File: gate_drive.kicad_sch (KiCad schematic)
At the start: 186 parts, among them J19 Conn_01x03, J20 Conn_01x03, Q1 Q_PNP_BEC, Q2 Q_PNP_BEC, Q3 Q_PNP_BEC, Q4 Q_PNP_BEC, Q5 Q_PNP_BEC, Q6 Q_PNP_BEC, U1 EG2131, U14 INA193, U2 EG2131, U20 INA193, U21 INA193, U22 INA193, U35 INA193, U36 INA826, U37 INA193, U38 INA826, U39 INA193, U4 EG2131, U40 INA826, U41 INA193, U42 INA826, U5 EG2131, U7 EG2131, U8 EG2131

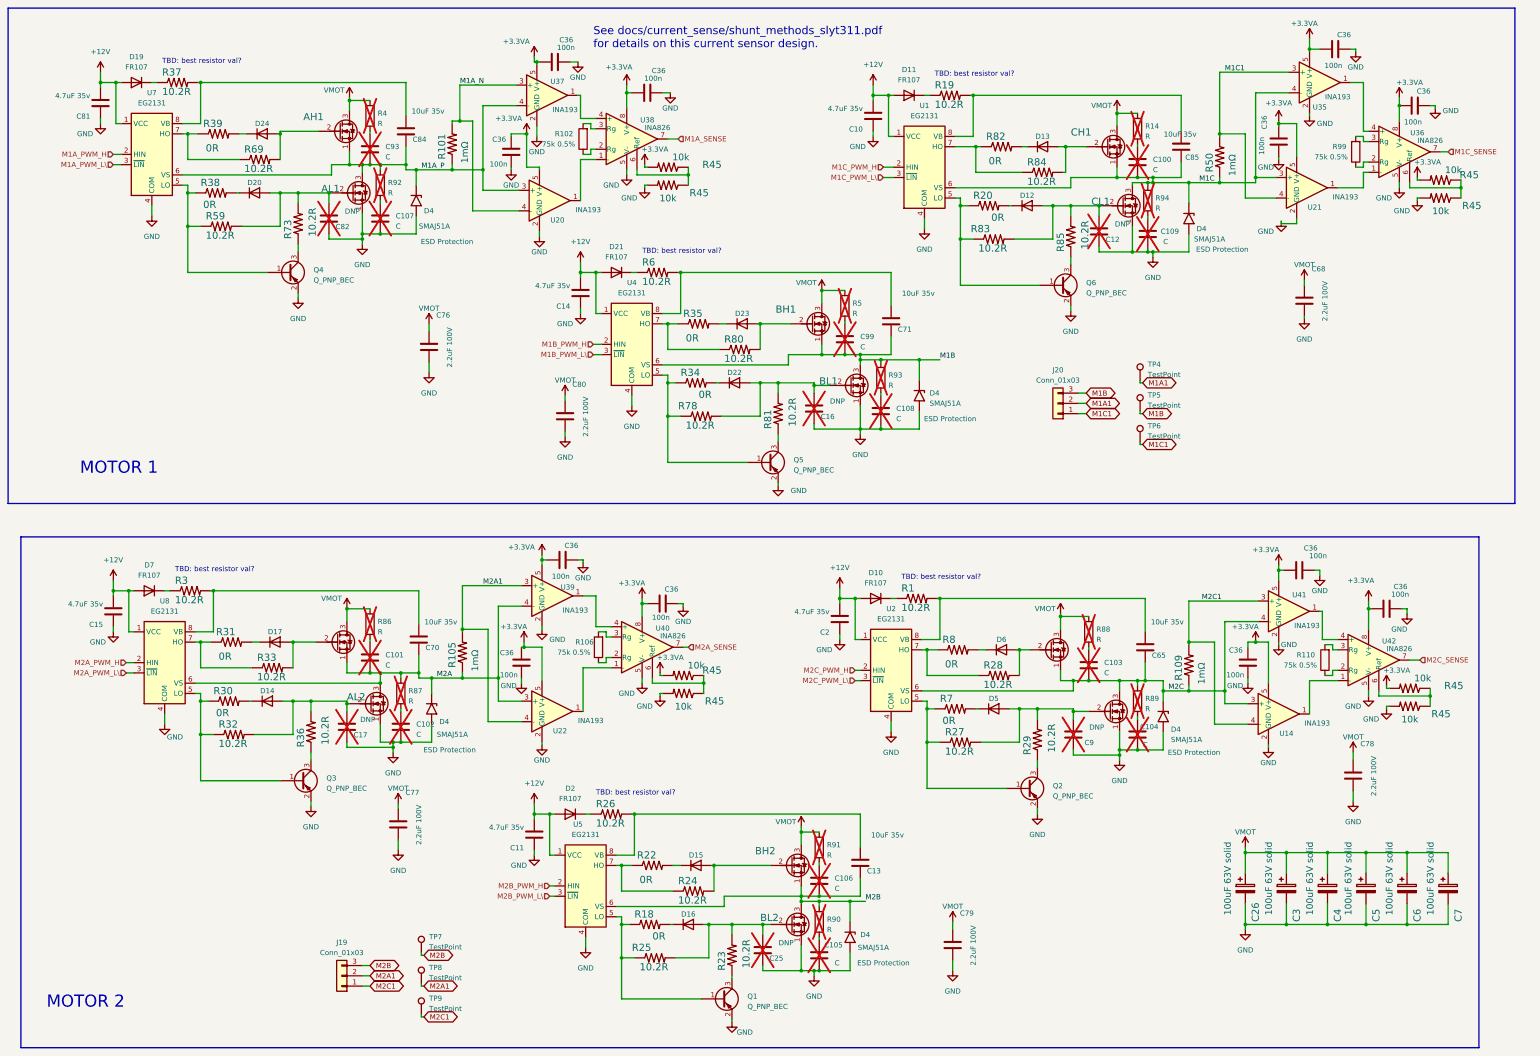
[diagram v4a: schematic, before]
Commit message: Work in progress. cleared out old traces in layout and starting fresh
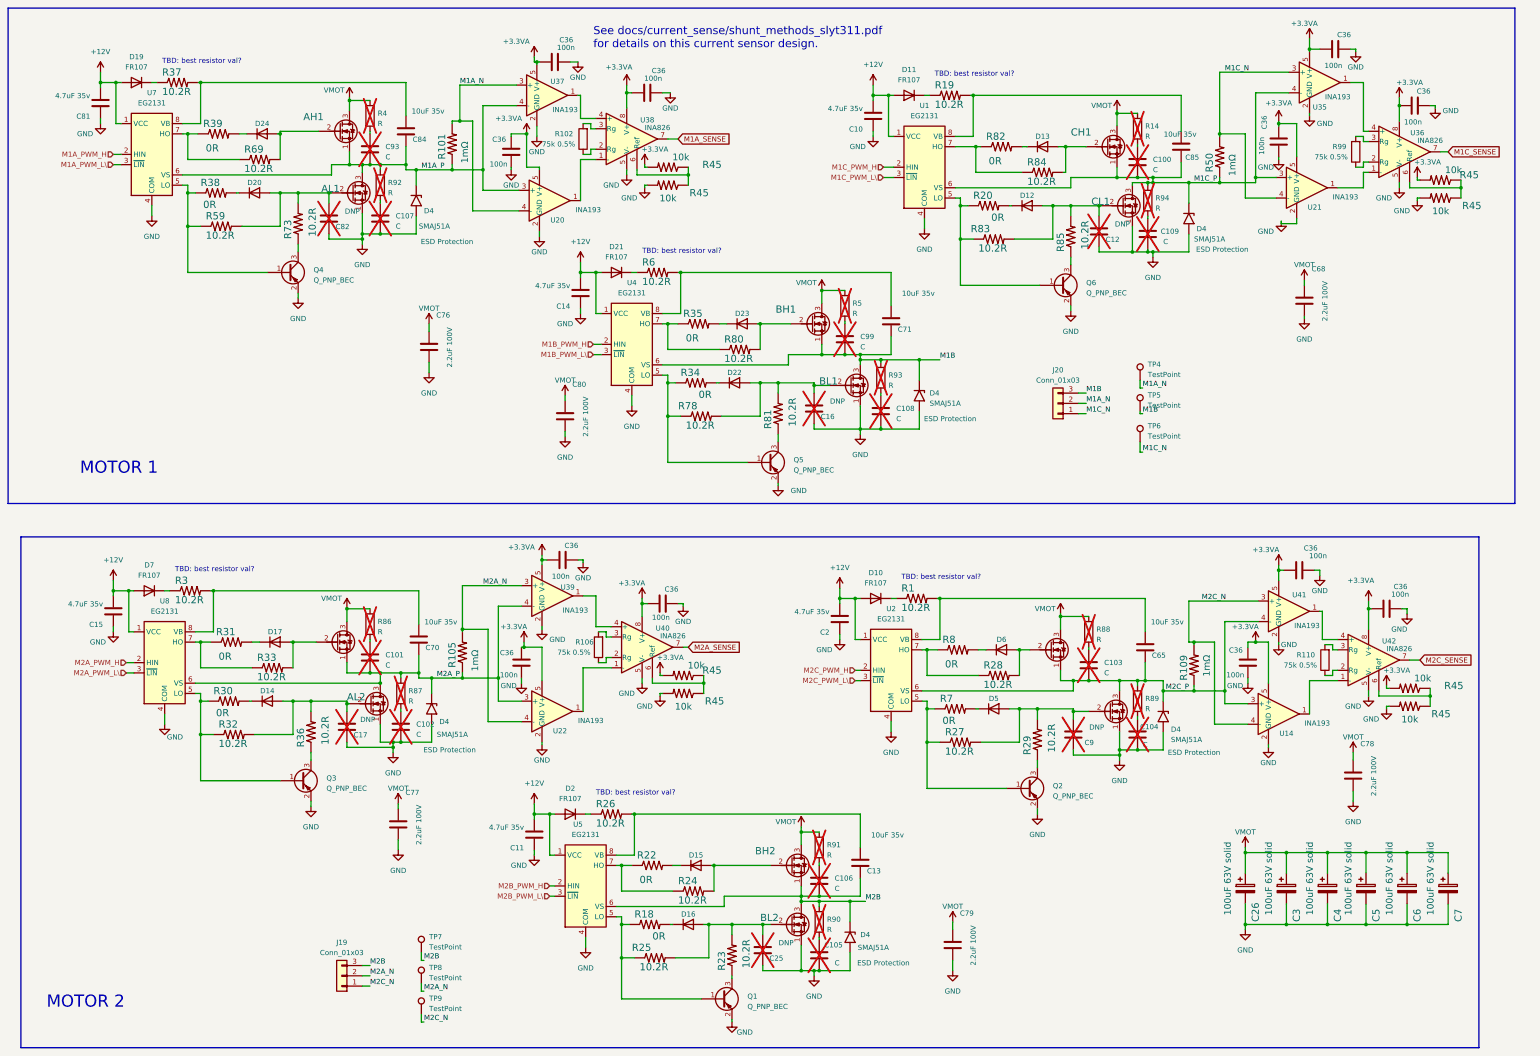
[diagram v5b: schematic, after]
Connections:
- net M1A1 is gone; now on net M1A_N: J20.2 (Pin_2), TP4.1
- net M1C renamed M1C_P
- net M1C1 renamed M1C_N
- net M2A renamed M2A_P
- net M2A1 renamed M2A_N
- net M2C renamed M2C_P
- net M2C1 renamed M2C_N
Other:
- moved on the sheet: R109

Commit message: Latest layout updates, with minor schematic changes.
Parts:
- added R113, R114, R115, R116: 2mΩ, Resistor_SMD:R_2512_6332Metric, symbol MotorController:TAYLOR_RESISTOR
- R101, R105, R109, R50: value 1mΩ -> 2mΩ; LCSC C5119465 -> C695813
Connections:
- net M1A_N: now also D4.1 (A1), R116.2
- net M1A_P: now also R116.1; no longer D4.1 (A1)
- net M1C_N: now also D4.1 (A1), R115.2
- net M1C_P: now also R115.1; no longer D4.1 (A1)
- net M2A_N: now also D4.1 (A1), R113.2
- net M2A_P: now also R113.1; no longer D4.1 (A1)
- net M2C_N: now also D4.1 (A1), R114.2
- net M2C_P: now also R114.1; no longer D4.1 (A1)
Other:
- moved on the sheet: D4, R101, R109

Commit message: Nearly complete layout now. Probably a functional design.
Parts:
- added JP2 (x4): SolderJumper_2_Open, Jumper:SolderJumper-2_P1.3mm_Open_RoundedPad1.0x1.5mm, symbol Jumper:SolderJumper_2_Open
- added R117, R118, R119, R120: 31.6k 1%, Resistor_SMD:R_0603_1608Metric, symbol Device:R
- D4: LCSC C173506 -> C726760
- J19, J20: now left out of the parts list
- U1, U2, U4, U5, U7, U8: value EG2131 -> EG3113; LCSC C5240691 -> C480666
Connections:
- net at R99.1, U36.2 (Rg): now also R117.1
- net at R99.2, U36.3 (Rg): now also JP2.2 (B)
- net at R110.1, U42.2 (Rg): now also R120.1
- net at R110.2, U42.3 (Rg): now also JP2.2 (B)
- net at R106.1, U40.2 (Rg): now also R119.1
- net at R106.2, U40.3 (Rg): now also JP2.2 (B)
- net at R102.1, U38.2 (Rg): now also R118.1
- net at R102.2, U38.3 (Rg): now also JP2.2 (B)
- new net: JP2.1 (A), R120.2
- new net: JP2.1 (A), R119.2
- new net: JP2.1 (A), R117.2
- new net: JP2.1 (A), R118.2
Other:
- note added: "Note: EG3113 or EG2131 gate drivers may be used."
- moved on the sheet: C36, R102, R106, R110, R45, U38, U40, U42

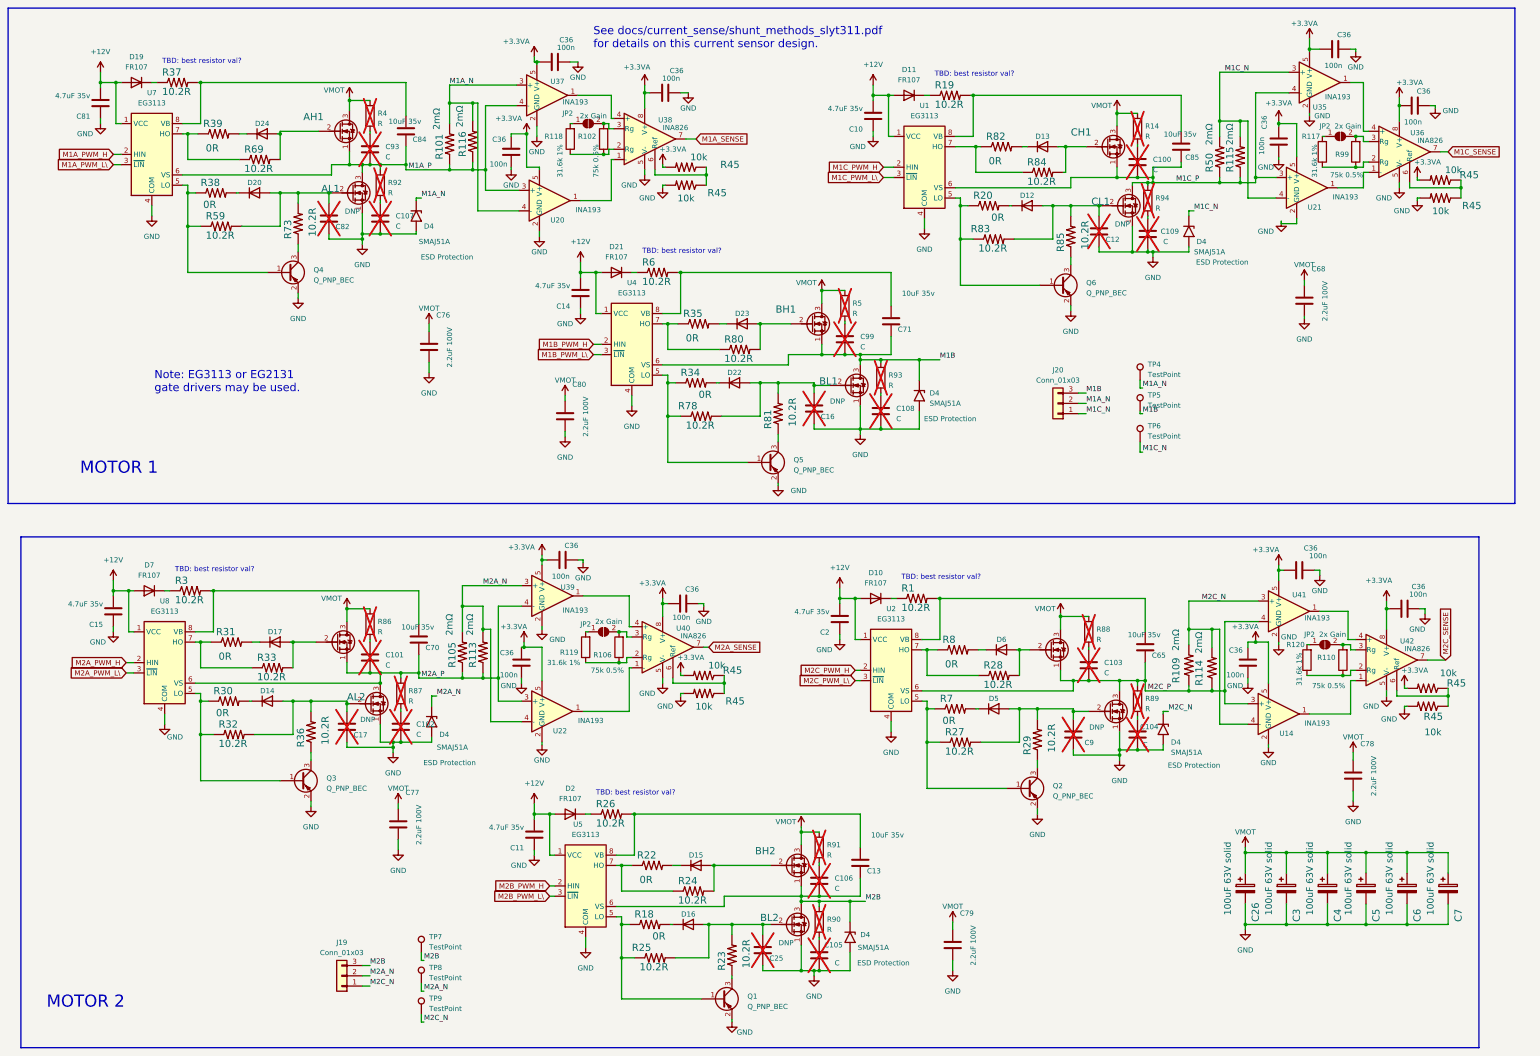
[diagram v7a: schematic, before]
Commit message: Added test points for full bridge and did light clean up on pcb.
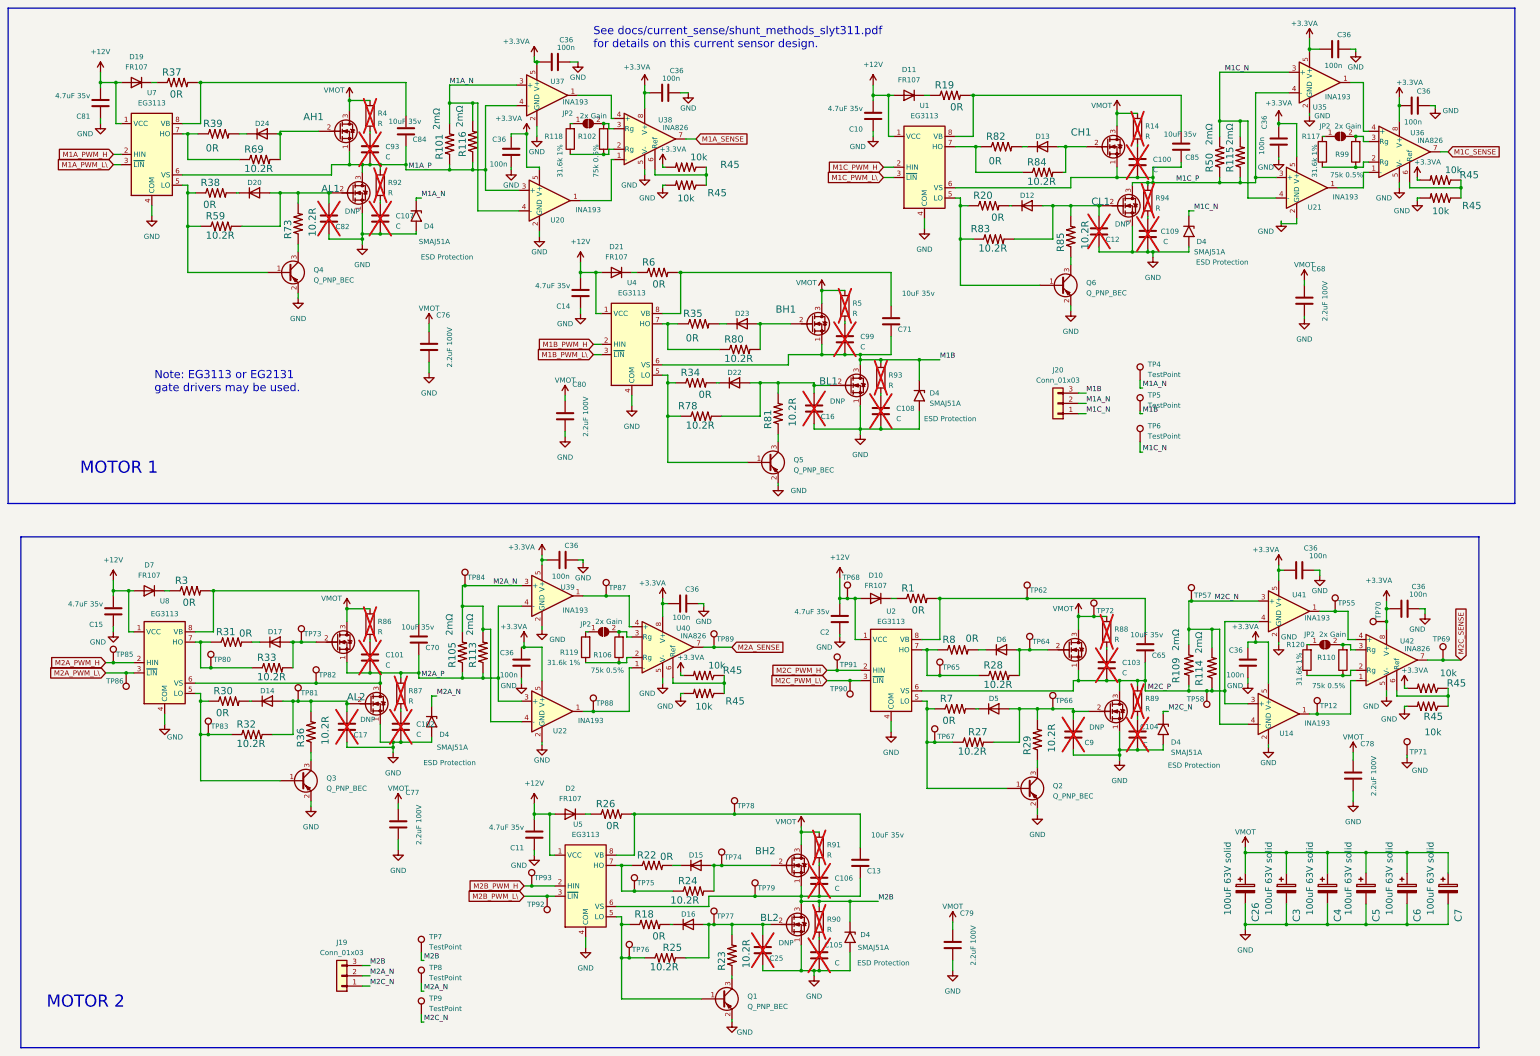
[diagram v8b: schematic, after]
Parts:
- added TP12, TP55, TP57, TP58, TP62, TP64, TP65, TP66, TP67, TP68, TP69, TP70, TP71, TP72, TP73, TP74, TP75, TP76, TP77, TP78, TP79, TP80, TP81, TP82, TP83, TP84, TP85, TP86, TP87, TP88, TP89, TP90, TP91, TP92, TP93: TestPoint, TestPoint:TestPoint_Pad_D1.5mm, symbol Connector:TestPoint
- AH1, AH2, AL1, AL2, BH1, BH2, BL1, BL2, CH1, CH2, CL1, CL2: LCSC C2908526 -> C454269
- R1, R19, R26, R3, R37, R6: value 10.2R -> 0R; LCSC C22773 -> C21189
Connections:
- net +12V: now also TP68.1
- net +3.3VA: now also TP70.1
- net GND: now also TP71.1
- net M2A_N: now also TP84.1
- net M2A_P: now also TP82.1
- net M2A_PWM_H: now also TP85.1
- net M2A_PWM_L\: now also TP86.1
- net M2A_SENSE: now also TP89.1
- net M2B: now also TP79.1
- net M2B_PWM_H: now also TP93.1
- net M2B_PWM_L\: now also TP92.1
- net M2C_N: now also TP57.1
- net M2C_P: now also TP58.1
- net M2C_PWM_H: now also TP91.1
- net M2C_PWM_L\: now also TP90.1
- net M2C_SENSE: now also TP69.1
- net VMOT: now also TP72.1
- net at C9.2, CL2.2 (G), D5.2 (A)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: now also TP66.1
- net at AH2.2 (G), D17.2 (A), R33.2: now also TP73.1
- net at C65.2, R1.2, U2.8 (VB): now also TP62.1
- net at BH2.2 (G), D15.2 (A), R24.2: now also TP74.1
- net at BL2.2 (G), C25.2, D16.2 (A)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: now also TP77.1
- net at Q3.1 (B), R30.1, R32.1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: now also TP83.1
- net at R31.1, R33.1, U8.7 (HO): now also TP80.1
- net at Q1.1 (B), R18.1, R25.1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: now also TP76.1
- net at R22.1, R24.1, U5.7 (HO): now also TP75.1
- net at C13.2, R26.2, U5.8 (VB): now also TP78.1
- net at CH2.2 (G), D6.2 (A), R28.2: now also TP64.1
- net at Q2.1 (B), R27.1, R7.1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: now also TP67.1
- net at U39.1, U40.4 (+): now also TP87.1
- net at AL2.2 (G), C17.2, D14.2 (A)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: now also TP81.1
- net at U22.1, U40.1 (-): now also TP88.1
- net at U41.1, U42.4 (+): now also TP55.1
- net at R28.1, R8.1, U2.7 (HO): now also TP65.1
- net at U14.1, U42.1 (-): now also TP12.1
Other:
- note removed: "TBD: best resistor val?"
- moved on the sheet: C103, R25, R27, R32, R88
